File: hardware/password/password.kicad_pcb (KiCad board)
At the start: 2 copper layers, 100 x 100 mm, 69 parts, among them J1 Conn_01x24_Male, J2 Conn_01x24_Male, SW1 SW_DIP_x01, SW10 SW_DIP_x01, SW11 SW_DIP_x01, SW12 SW_DIP_x01, SW13 SW_DIP_x01, SW2 SW_DIP_x01, SW4 SW_DIP_x01, SW5 SW_DIP_x01, SW6 SW_DIP_x01, SW7 SW_DIP_x01, SW8 SW_DIP_x01

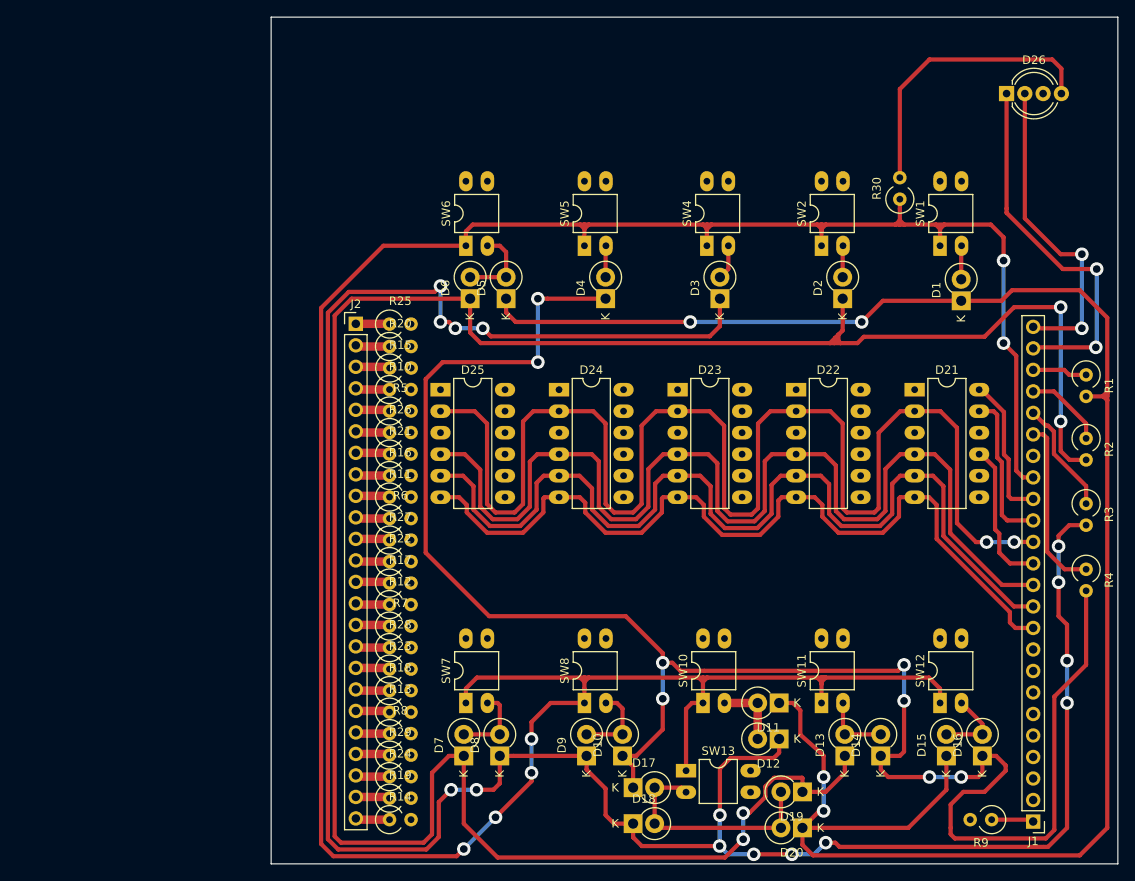
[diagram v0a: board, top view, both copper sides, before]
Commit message: Add copper fills
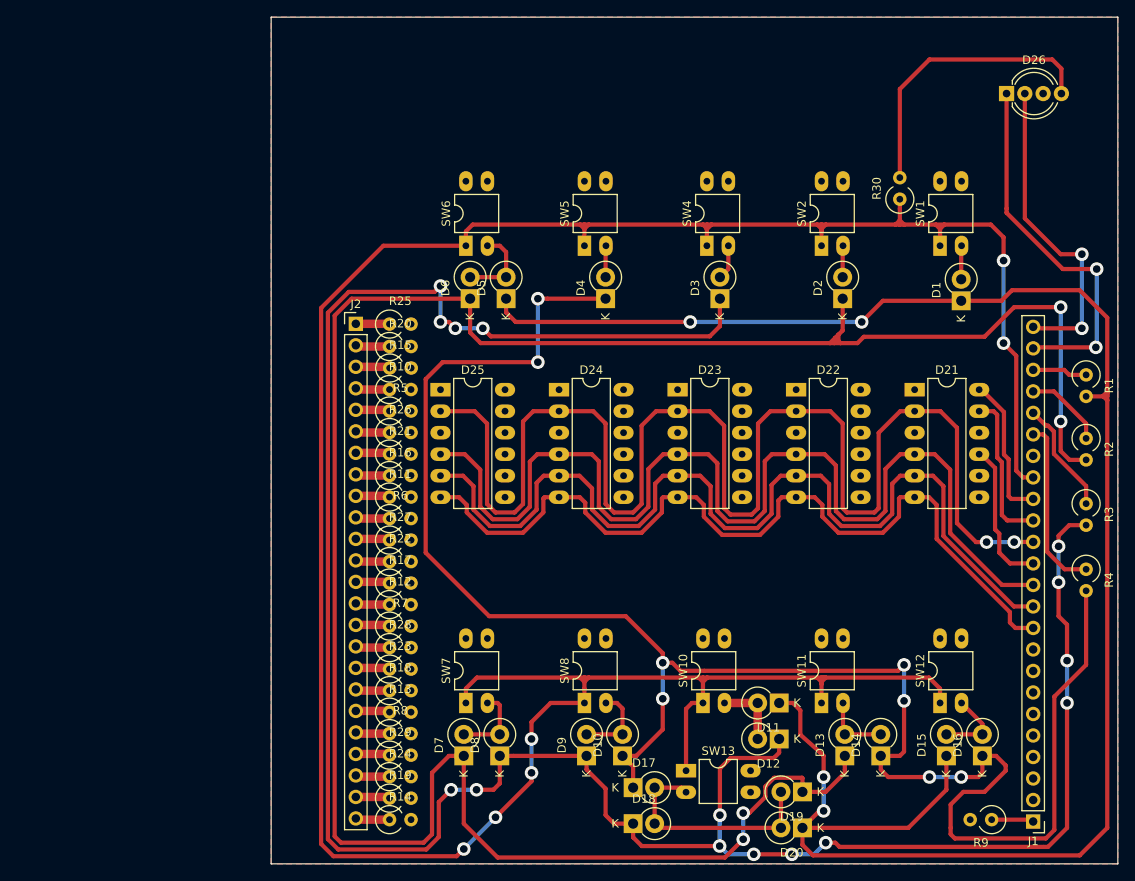
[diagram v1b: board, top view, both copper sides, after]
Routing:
- added copper zone on F.Cu, net (none)
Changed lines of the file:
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@@
     (user_trace_width 1)
     (trace_clearance 0.3)
-    (zone_clearance 0.508)
+    (zone_clearance 0.7)
     (zone_45_only no)
     (trace_min 0.2)
@@
   (segment (start 173.332001 56.082001) (end 173.332001 59.025001) (width 0.5) (layer F.Cu) (net 80))
   (segment (start 172.25 55) (end 173.332001 56.082001) (width 0.5) (layer F.Cu) (net 80))
+  (zone (net 0) (net_name "") (layer F.Cu) (hatch edge 0.508)
+    (connect_pads (clearance 0.7))
+    (min_thickness 1)
+    (fill yes (arc_segments 32) (thermal_gap 0.508) (thermal_bridge_width 1.01))
+    (polygon
+      (pts
+        (xy 180 150) (xy 80 150) (xy 80 50) (xy 180 50)
+      )
+    )
+  )
 )

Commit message: Create single-board Password PCB
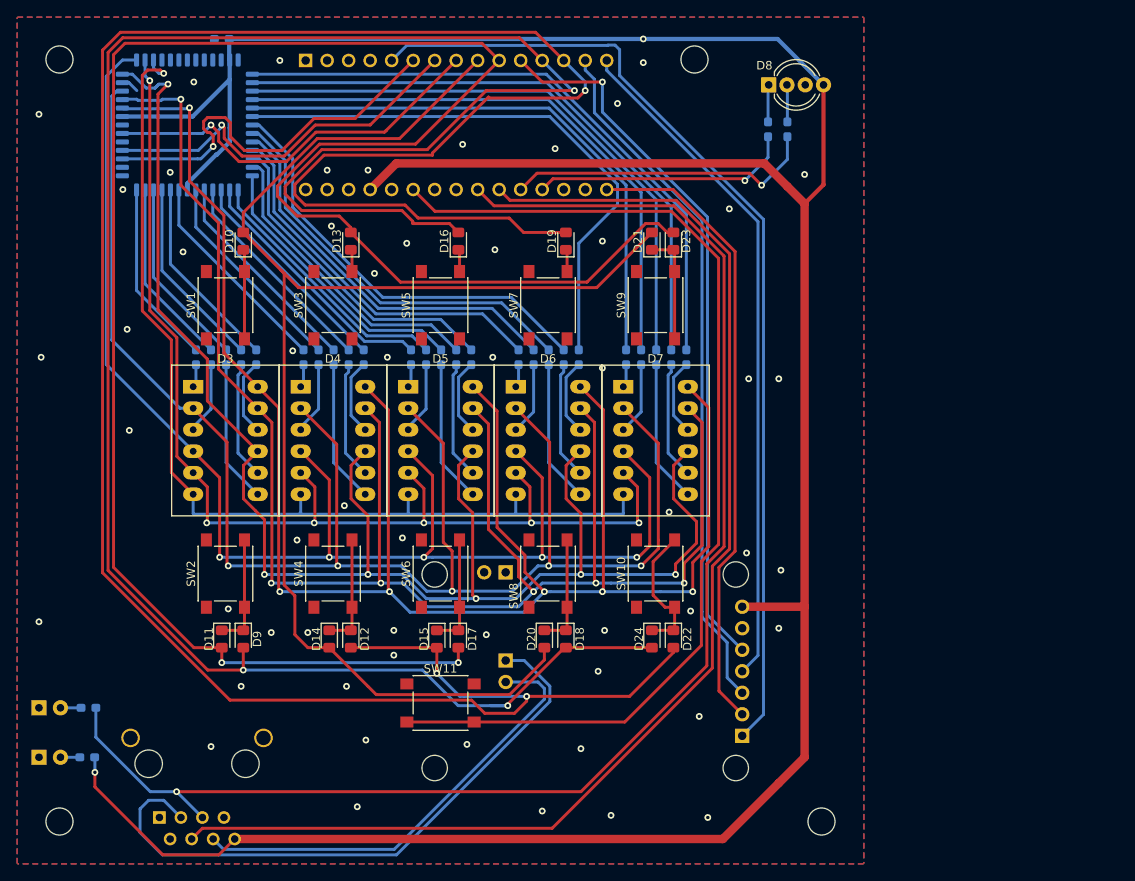
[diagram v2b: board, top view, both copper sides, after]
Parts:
- removed D25: 7x5LedMatrix, Package_DIP:DIP-12_W7.62mm_LongPads
- removed D26: LED_RGBA, LED_THT:LED_D5.0mm-4_RGB_Wide_Pins
- removed J2: Conn_01x24_Male, Connector_PinHeader_2.54mm:PinHeader_1x24_P2.54mm_Vertical
- removed R30: 220R, Resistor_THT:R_Axial_DIN0309_L9.0mm_D3.2mm_P2.54mm_Vertical
- removed SW12, SW13: SW_DIP_x01, Package_DIP:DIP-4_W7.62mm_LongPads
- added A1: Arduino_Nano_v3.x, Module:Arduino_Nano, B.Cu at (84.1, 55.1)
- added C1: 0.1uF, Capacitor_SMD:C_0603_1608Metric_Pad1.05x0.95mm_HandSolder, B.Cu at (74.2, 52.6)
- added REF**: MountingHole_3.2mm_M3, MountingHole:MountingHole_3.2mm_M3, F.Cu at (130.0, 55.0)
- added REF**: MountingHole_3.2mm_M3, MountingHole:MountingHole_3.2mm_M3, F.Cu at (145.0, 145.0)
- added REF**: MountingHole_3.2mm_M3, MountingHole:MountingHole_3.2mm_M3, F.Cu at (55.0, 145.0)
- added REF**: MountingHole_3.2mm_M3, MountingHole:MountingHole_3.2mm_M3, F.Cu at (55.0, 55.0)
- added SW3: SW_DIP_x01, Button_Switch_SMD:SW_Push_1P1T_NO_6x6mm_H9.5mm, F.Cu at (87.3, 84.0)
- added SW9: SW_DIP_x01, Button_Switch_SMD:SW_Push_1P1T_NO_6x6mm_H9.5mm, F.Cu at (125.4, 84.0)
- added U1: WAVGAT_CAN, WAVGAT_CAN:WAVGAT_CAN, B.Cu at (127.0, 110.5)
- added U2: HT1632C-52LQFP, Package_QFP:LQFP-52_14x14mm_P1mm, B.Cu at (70.1, 62.7)
- D1, D2: value D -> LED_Small; footprint Diode_THT:D_DO-15_P2.54mm_Vertical_KathodeUp -> LED_THT:LED_D3.0mm; moved to B.Cu
- D10, D11, D12, D13, D14, D15, D16, D17, D18, D19, D20, D9: footprint Diode_THT:D_DO-15_P2.54mm_Vertical_KathodeUp -> Diode_SMD:D_0805_2012Metric_Pad1.15x1.40mm_HandSolder
- D21, D22, D23, D24: value 7x5LedMatrix -> D; footprint Package_DIP:DIP-12_W7.62mm_LongPads -> Diode_SMD:D_0805_2012Metric_Pad1.15x1.40mm_HandSolder
- D3, D4, D5, D6, D7: value D -> 7x5LedMatrix; footprint Diode_THT:D_DO-15_P2.54mm_Vertical_KathodeUp -> ProjectDisplays:LMD07057BAG
- D8: value D -> LED_RGBA; footprint Diode_THT:D_DO-15_P2.54mm_Vertical_KathodeUp -> LED_THT:LED_D5.0mm-4_RGB_Wide_Pins
- J1: value Conn_01x24_Male -> RJ45_Shielded; footprint Connector_PinHeader_2.54mm:PinHeader_1x24_P2.54mm_Vertical -> RJ45_5224:RJ45_5224; moved to B.Cu
- R1, R2: value 1K -> 560R; footprint Resistor_THT:R_Axial_DIN0309_L9.0mm_D3.2mm_P2.54mm_Vertical -> Resistor_SMD:R_0603_1608Metric_Pad1.05x0.95mm_HandSolder; moved to B.Cu
- R10, R11, R12, R13, R14, R15, R16, R17, R18, R19, R20, R21, R22, R23, R24, R25, R26, R27, R28, R29, R5, R6, R7, R8, R9: footprint Resistor_THT:R_Axial_DIN0309_L9.0mm_D3.2mm_P2.54mm_Vertical -> Resistor_SMD:R_0603_1608Metric_Pad1.05x0.95mm_HandSolder; moved to B.Cu
- R3, R4: value 1K -> 220R; footprint Resistor_THT:R_Axial_DIN0309_L9.0mm_D3.2mm_P2.54mm_Vertical -> Resistor_SMD:R_0603_1608Metric_Pad1.05x0.95mm_HandSolder; moved to B.Cu
- SW1, SW10, SW11, SW2, SW4, SW5, SW6, SW7, SW8: footprint Package_DIP:DIP-4_W7.62mm_LongPads -> Button_Switch_SMD:SW_Push_1P1T_NO_6x6mm_H9.5mm
- moved R1 126.3 mm to (58.3, 137.4), turned to 180 degrees
- moved R2 122.1 mm to (58.4, 131.6), turned to 0 degrees
- moved D1 121.5 mm to (52.6, 137.4), turned to 0 degrees
- moved D2 106.5 mm to (52.6, 131.6), turned to 0 degrees
- moved R4 104.6 mm to (74.7, 90.2)
- moved J1 103.2 mm to (66.8, 144.5), turned to 0 degrees
- moved R3 101.3 mm to (76.5, 90.2)
- moved R9 95.0 mm to (87.4, 90.2), turned to 270 degrees
- moved R29 87.6 mm to (141.0, 63.2), turned to 270 degrees
- moved D16 86.8 mm to (102.1, 76.5)
- moved D8 85.4 mm to (138.8, 58.0), turned to 0 degrees
- moved SW1 84.7 mm to (74.6, 84.0)
- moved D13 84.3 mm to (89.4, 76.5)
- moved SW2 80.3 mm to (74.6, 115.7)
- moved R28 75.8 mm to (138.7, 63.2), turned to 270 degrees
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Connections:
- D1 pad 1: Net-(D1-Pad1) -> GND
- D10 pad 2: Net-(D10-Pad2) -> D6
- D11 pad 1: Net-(D1-Pad1) -> Net-(D11-Pad1)
- D11 pad 2: Net-(D11-Pad2) -> D7
- D12 pad 2: Net-(D11-Pad2) -> D10
- D13 pad 2: Net-(D13-Pad2) -> D7
- D14 pad 1: Net-(D10-Pad1) -> Net-(D12-Pad1)
- D14 pad 2: Net-(D13-Pad2) -> D6
- D15 pad 1: Net-(D1-Pad1) -> Net-(D15-Pad1)
- D15 pad 2: Net-(D15-Pad2) -> D10
- D16 pad 1: Net-(D10-Pad1) -> Net-(D16-Pad1)
- D16 pad 2: Net-(D15-Pad2) -> D9
- D17 pad 1: Net-(D10-Pad1) -> Net-(D15-Pad1)
- D17 pad 2: Net-(D17-Pad2) -> D7
- D18 pad 1: Net-(D12-Pad1) -> Net-(D18-Pad1)
- D18 pad 2: Net-(D17-Pad2) -> D9
- D19 pad 1: Net-(D13-Pad1) -> Net-(D19-Pad1)
- D19 pad 2: Net-(D17-Pad2) -> D10
- D2 pad 1: Net-(D13-Pad1) -> GND
- D20 pad 1: Net-(D1-Pad1) -> Net-(D18-Pad1)
- D20 pad 2: Net-(D17-Pad2) -> D6
- D21 pad 2: Net-(D21-Pad2) -> D6
- D22 pad 2: Net-(D21-Pad2) -> D10
- D23 pad 1: Net-(D23-Pad1) -> Net-(D21-Pad1)
- D23 pad 2: Net-(D21-Pad2) -> D7
- D24 pad 1: Net-(D24-Pad1) -> Net-(D22-Pad1)
- D24 pad 2: Net-(D21-Pad2) -> D9
- D3 pad 1: Net-(D12-Pad1) -> Net-(D3-Pad1)
- D4 pad 1: Net-(D10-Pad1) -> Net-(D4-Pad1)
- D4 pad 2: Net-(D4-Pad2) -> Net-(D3-Pad2)
- D5 pad 1: Net-(D1-Pad1) -> Net-(D5-Pad1)
- D5 pad 2: Net-(D5-Pad2) -> Net-(D3-Pad2)
- D6 pad 1: Net-(D13-Pad1) -> Net-(D6-Pad1)
- D6 pad 2: Net-(D5-Pad2) -> Net-(D3-Pad2)
- D7 pad 1: Net-(D13-Pad1) -> Net-(D7-Pad1)
- D7 pad 2: Net-(D7-Pad2) -> Net-(D3-Pad2)
- D8 pad 1: Net-(D12-Pad1) -> Net-(D8-Pad1)
- D8 pad 2: Net-(D7-Pad2) -> Net-(D8-Pad2)
- D9 pad 1: Net-(D12-Pad1) -> Net-(D11-Pad1)
- D9 pad 2: Net-(D10-Pad2) -> D9
- J1 pad 1: Net-(J1-Pad1) -> GND
- J1 pad 2: (no net) -> +12V
- J1 pad 3: (no net) -> Net-(J1-Pad3)
- J1 pad 4: (no net) -> MODULE_READY
- J1 pad 5: (no net) -> MODULE_ENABLE
- J1 pad 6: (no net) -> Net-(J1-Pad6)
- J1 pad 7: (no net) -> GND
- J1 pad 8: (no net) -> VCC
- R1 pad 1: Net-(J1-Pad22) -> VCC
- R1 pad 2: Net-(D1-Pad1) -> Net-(D1-Pad2)
- R10 pad 2: Net-(D21-Pad7) -> Net-(D4-Pad10)
- R11 pad 2: Net-(D22-Pad7) -> Net-(D4-Pad3)
- R12 pad 2: Net-(D23-Pad7) -> Net-(D4-Pad1)
- R13 pad 2: Net-(D24-Pad7) -> Net-(D5-Pad8)
- R14 pad 2: Net-(D25-Pad7) -> Net-(D5-Pad7)
- R15 pad 2: Net-(D21-Pad10) -> Net-(D5-Pad10)
- R16 pad 2: Net-(D22-Pad10) -> Net-(D5-Pad3)
- R17 pad 2: Net-(D23-Pad10) -> Net-(D5-Pad1)
- R18 pad 2: Net-(D24-Pad10) -> Net-(D6-Pad8)
- R19 pad 2: Net-(D25-Pad10) -> Net-(D6-Pad7)
- R2 pad 1: Net-(J1-Pad21) -> Net-(D2-Pad2)
- R2 pad 2: Net-(D13-Pad1) -> MODULE_ENABLE
- R20 pad 2: Net-(D21-Pad3) -> Net-(D6-Pad10)
- R21 pad 2: Net-(D22-Pad3) -> Net-(D6-Pad3)
- R22 pad 2: Net-(D23-Pad3) -> Net-(D6-Pad1)
- R23 pad 2: Net-(D24-Pad3) -> Net-(D7-Pad8)
- R24 pad 2: Net-(D25-Pad3) -> Net-(D7-Pad7)
- R25 pad 2: Net-(D21-Pad1) -> Net-(D7-Pad10)
- R26 pad 2: Net-(D22-Pad1) -> Net-(D7-Pad3)
- R27 pad 2: Net-(D23-Pad1) -> Net-(D7-Pad1)
- R28 pad 1: Net-(J2-Pad16) -> Net-(D8-Pad1)
- R28 pad 2: Net-(D24-Pad1) -> A0
- R29 pad 1: Net-(J2-Pad21) -> Net-(D8-Pad2)
- R29 pad 2: Net-(D25-Pad1) -> A1
- R3 pad 1: Net-(J1-Pad20) -> Net-(R3-Pad1)
- R3 pad 2: Net-(D12-Pad1) -> Net-(D3-Pad8)
- R4 pad 1: Net-(J1-Pad19) -> Net-(R4-Pad1)
- R4 pad 2: Net-(D10-Pad1) -> Net-(D3-Pad7)
- R5 pad 2: Net-(D21-Pad8) -> Net-(D3-Pad10)
- R6 pad 2: Net-(D22-Pad8) -> Net-(D3-Pad3)
- R7 pad 2: Net-(D23-Pad8) -> Net-(D3-Pad1)
- R8 pad 2: Net-(D24-Pad8) -> Net-(D4-Pad8)
- R9 pad 1: Net-(J1-Pad1) -> Net-(R9-Pad1)
- R9 pad 2: Net-(D25-Pad8) -> Net-(D4-Pad7)
- SW1 pad 1: VCC -> GND
- SW1 pad 2: Net-(D1-Pad2) -> Net-(D10-Pad1)
- SW10 pad 1: VCC -> GND
- SW10 pad 2: Net-(D11-Pad2) -> Net-(D22-Pad1)
- SW11 pad 1: VCC -> GND
- SW11 pad 2: Net-(D13-Pad2) -> A6
- SW2 pad 1: VCC -> GND
- SW2 pad 2: Net-(D2-Pad2) -> Net-(D11-Pad1)
- SW4 pad 1: VCC -> GND
- SW4 pad 2: Net-(D3-Pad2) -> Net-(D12-Pad1)
- SW5 pad 1: VCC -> GND
- SW5 pad 2: Net-(D4-Pad2) -> Net-(D16-Pad1)
- SW6 pad 1: VCC -> GND
- SW6 pad 2: Net-(D5-Pad2) -> Net-(D15-Pad1)
- SW7 pad 1: VCC -> GND
- SW7 pad 2: Net-(D7-Pad2) -> Net-(D19-Pad1)
- SW8 pad 1: VCC -> GND
- SW8 pad 2: Net-(D10-Pad2) -> Net-(D18-Pad1)
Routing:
- net D10: track 0.00 -> 300.4 mm, vias 0 -> 3
- net Net-(D13-Pad1): track 272.7 -> 2.62 mm, vias 4 -> 0
- net Net-(D12-Pad1): track 282.7 -> 13.3 mm, vias 15 -> 0
- net D9: track 0.00 -> 262.4 mm, vias 0 -> 3
- net D7: track 0.00 -> 243.8 mm, vias 0 -> 2
- net Net-(D3-Pad12): track 0.00 -> 224.9 mm, vias 0 -> 6
- net Net-(D1-Pad1): track 222.4 -> 0.00 mm, vias 4 -> 0
- net Net-(D10-Pad1): track 220.7 -> 10.6 mm, vias 8 -> 0
- net Net-(D3-Pad11): track 0.00 -> 209.6 mm, vias 0 -> 6
- net Net-(D3-Pad2): track 4.14 -> 200.5 mm, vias 0 -> 5
- net Net-(D3-Pad9): track 0.00 -> 191.1 mm, vias 0 -> 6
- net Net-(D3-Pad4): track 0.00 -> 172.4 mm, vias 0 -> 5
- net D6: track 0.00 -> 170.4 mm
- net MODULE_ENABLE: track 0.00 -> 170.4 mm, vias 0 -> 1
- net Net-(D21-Pad2): track 167.7 -> 0.00 mm, vias 2 -> 0
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- added copper zone on B.Cu, net GND
- added copper zone on F.Cu, net GND
- removed copper zone on F.Cu, net (none)
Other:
- board outline removed

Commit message: Password PCB: spread letters apart and reroute
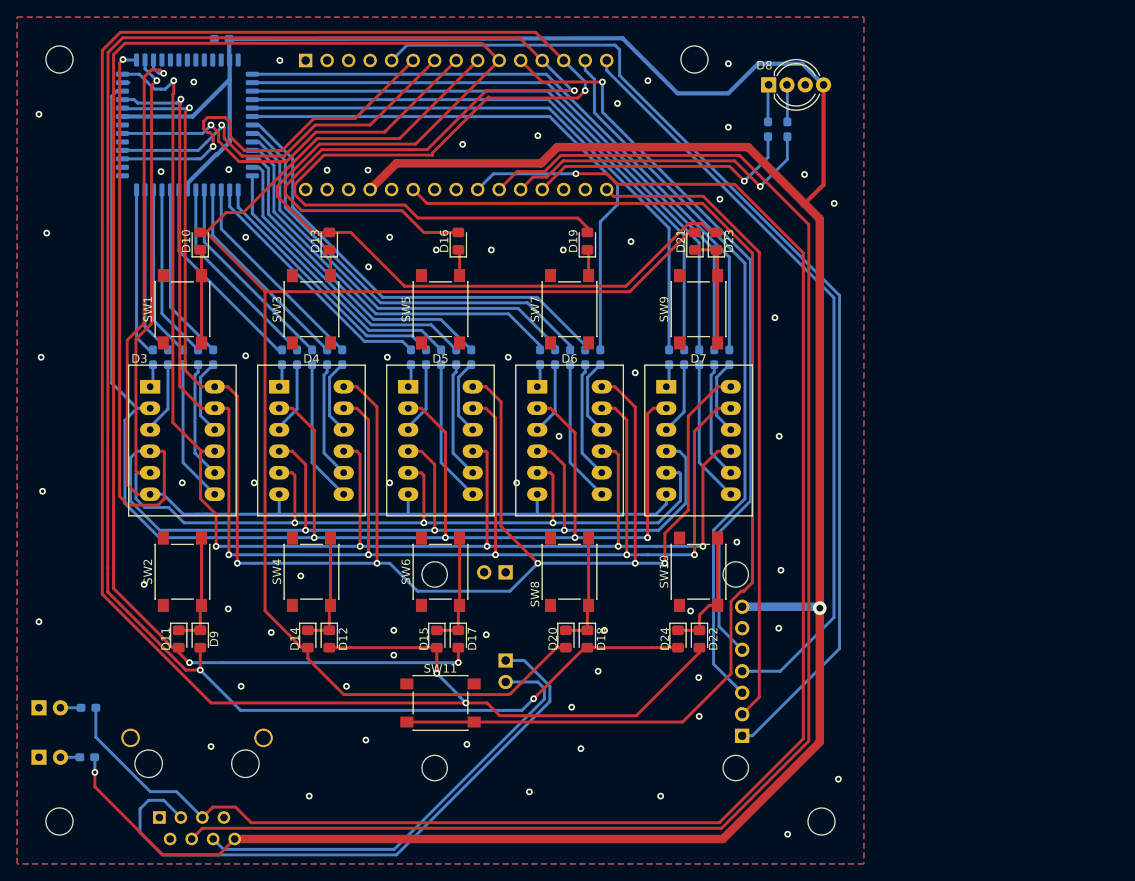
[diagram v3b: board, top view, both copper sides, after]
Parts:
- moved SW1 5.10 mm to (69.5, 84.5)
- moved SW9 5.10 mm to (130.5, 84.5)
- moved SW2 5.08 mm to (69.5, 115.5)
- moved SW10 5.08 mm to (130.5, 115.5)
- moved D11 5.08 mm to (69.1, 123.4)
- moved D3 5.08 mm to (65.7, 93.7)
- moved R24 5.08 mm to (130.6, 90.2)
- moved D10 5.08 mm to (71.6, 76.5)
- moved D21 5.08 mm to (130.0, 76.5)
- moved D23 5.08 mm to (132.6, 76.5)
- moved D7 5.08 mm to (126.7, 93.7)
- moved D9 5.08 mm to (71.6, 123.4)
- moved R23 5.08 mm to (132.3, 90.2)
- moved R26 5.08 mm to (128.8, 90.2)
- moved R27 5.08 mm to (127.0, 90.2)
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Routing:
- net MODULE_READY: track 150.0 -> 180.3 mm
- net MODULE_ENABLE: track 170.4 -> 196.8 mm
- net Net-(D3-Pad5): track 135.5 -> 150.9 mm, vias 6 -> 4
- net Net-(D3-Pad9): track 191.1 -> 175.7 mm
- net D6: track 170.4 -> 185.1 mm
- net Net-(D3-Pad2): track 200.5 -> 187.4 mm, vias 5 -> 4
- net Net-(D3-Pad4): track 172.4 -> 185.4 mm, vias 5 -> 4
- net Net-(D3-Pad11): track 209.6 -> 198.7 mm
- net A6: track 124.5 -> 134.7 mm
- net Net-(D3-Pad6): track 120.1 -> 130.2 mm
- net MISO: track 80.3 -> 90.4 mm
- net Net-(D3-Pad12): track 224.9 -> 216.3 mm
- net Net-(A1-Pad5): track 117.0 -> 125.1 mm
- net VCC: track 344.6 -> 352.5 mm
- net D7: track 243.8 -> 249.7 mm
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
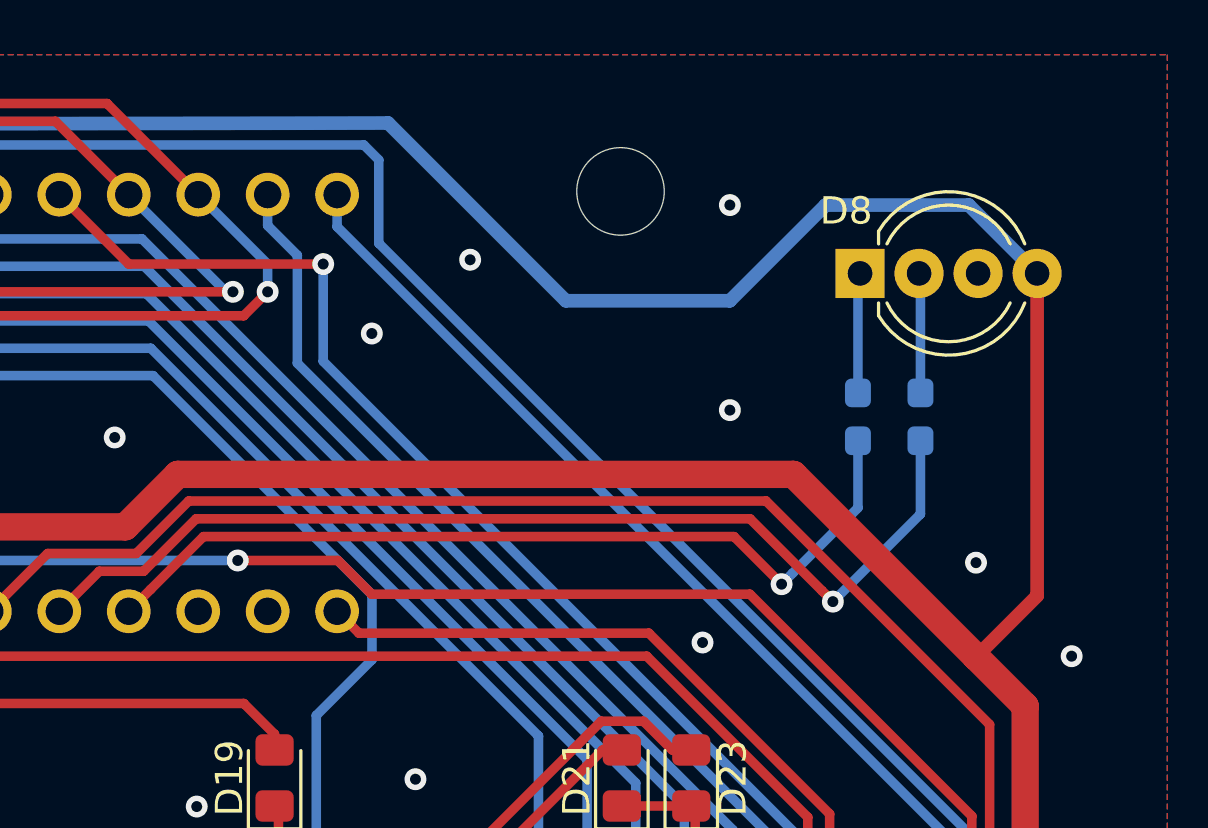
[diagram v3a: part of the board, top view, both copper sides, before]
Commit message: Password PCB: switch to correct RGB LED symbol
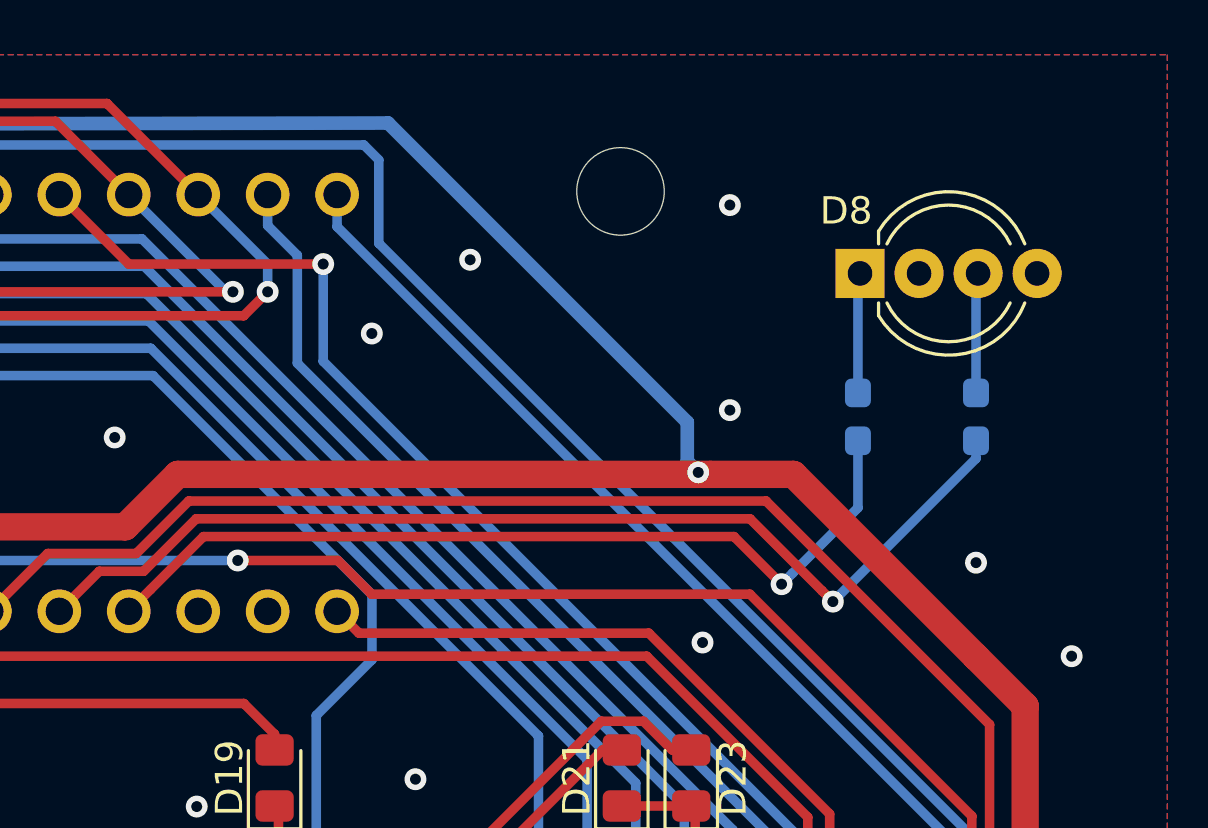
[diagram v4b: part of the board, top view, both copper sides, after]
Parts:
- D8: value LED_RGBA -> LED_RCGB
- moved R29 2.03 mm to (143.0, 63.2)
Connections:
- D8 pad 2: Net-(D8-Pad2) -> GND
- D8 pad 4: VCC -> Net-(D8-Pad4)
- R29 pad 1: Net-(D8-Pad2) -> Net-(D8-Pad3)
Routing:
- net VCC: track 352.5 -> 326.6 mm, vias 2 -> 3
- net Net-(D8-Pad3): track 0.00 -> 4.40 mm
- net Net-(D8-Pad2): track 4.39 -> 0.00 mm
- net A1: track 38.2 -> 39.0 mm

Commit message: Clean up symbol libraries, delete outdated files
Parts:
- D3, D4, D5, D6, D7: value 7x5LedMatrix -> LMD07057BAG

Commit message: Add missing copper fills and edge cuts
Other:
- board outline added: 100 x 100 mm

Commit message: Add identifying silkscreen text, fix missing connections on ModuleBase
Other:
- board text added: "BGame Password v1.0 PurkkaKoodari 2020"
